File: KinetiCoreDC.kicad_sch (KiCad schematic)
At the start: 7 parts, among them J2 TC2070-IDC-NL, SW1 PTS647, U1 STM32G070KBT6

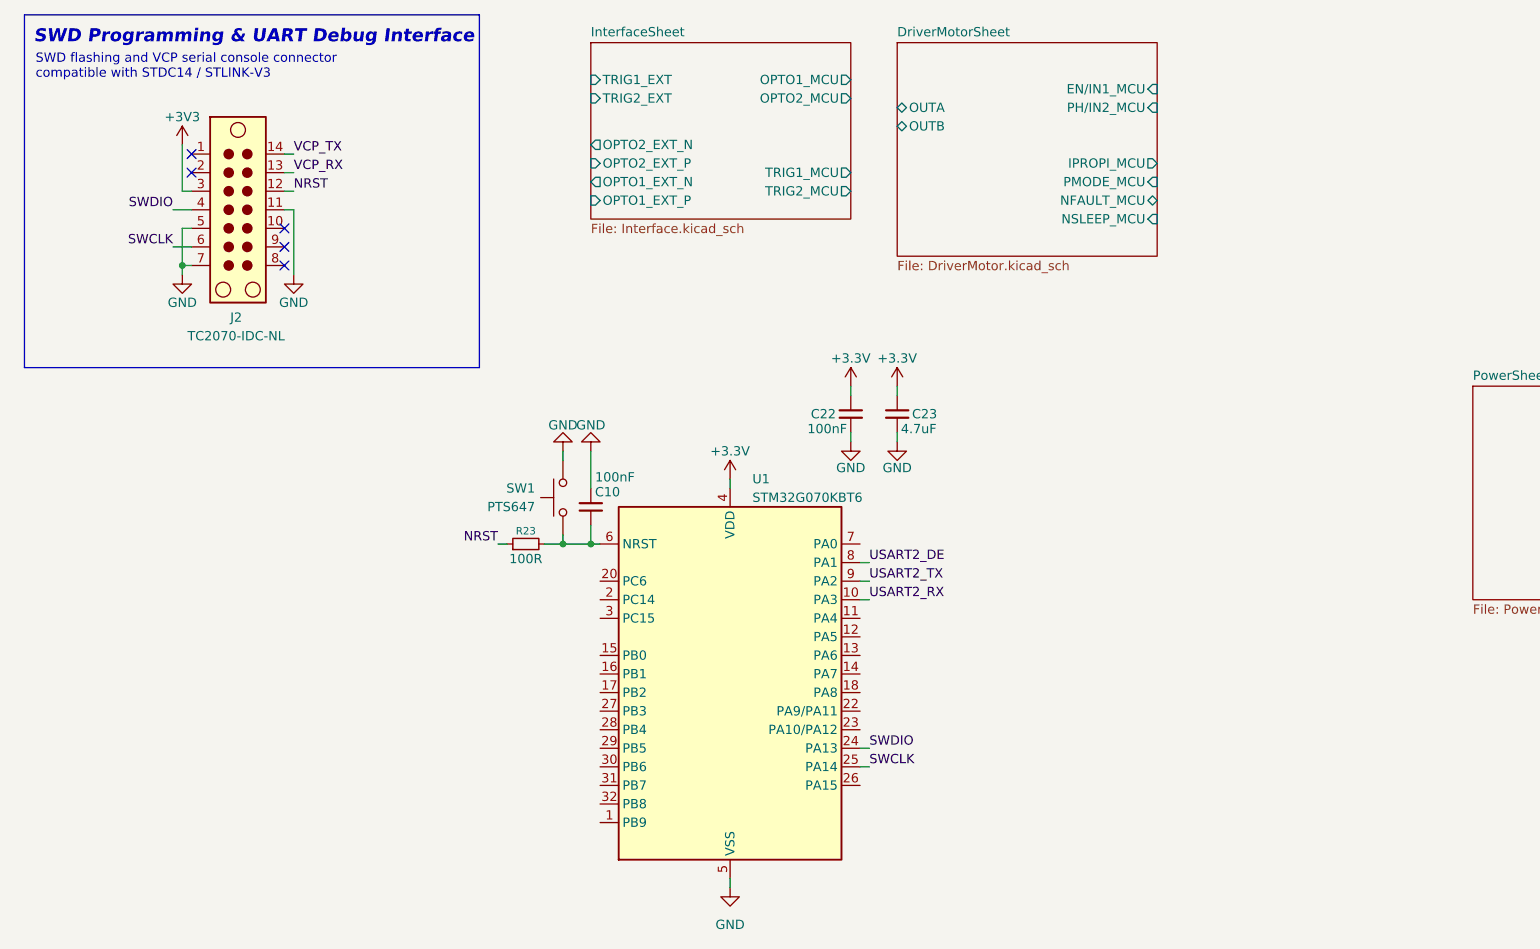
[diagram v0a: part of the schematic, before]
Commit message: feat: add LTC4365 protection circuit and 3.3V logic LDO
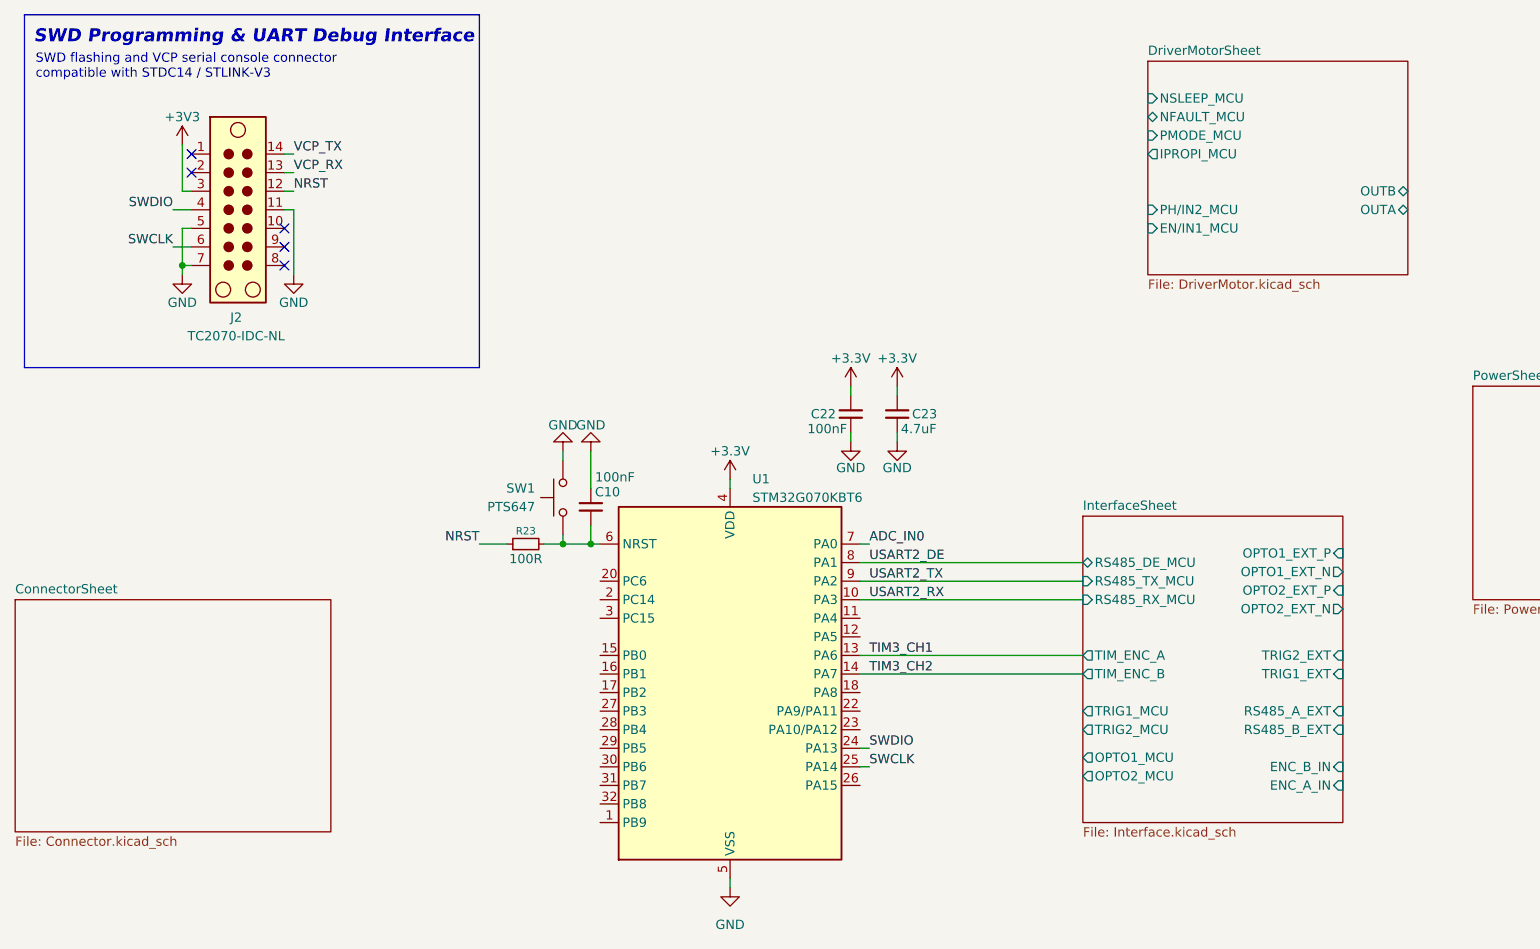
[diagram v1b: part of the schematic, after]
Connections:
- net TIM3_CH1: now reaches U1.13 (PA6)
- net TIM3_CH2: now reaches U1.14 (PA7)
- net ADC_IN0: now reaches U1.7 (PA0)
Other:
- added sheet ConnectorSheet (Connector.kicad_sch)
- sheet InterfaceSheet ports: added ENC_A_IN, ENC_B_IN, RS485_A_EXT, RS485_B_EXT, RS485_DE_MCU, RS485_RX_MCU, RS485_TX_MCU, TIM_ENC_A, TIM_ENC_B; removed none

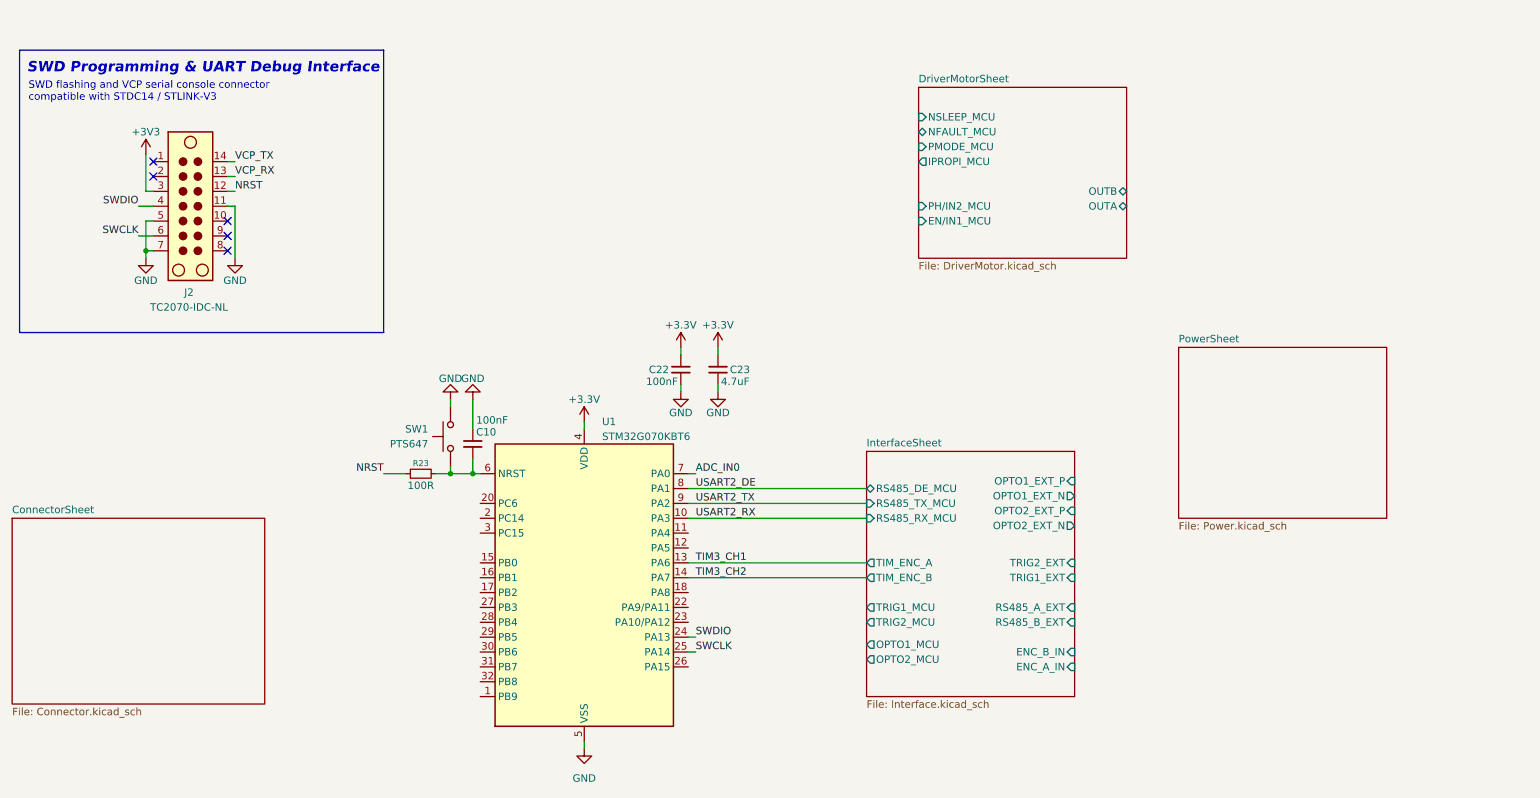
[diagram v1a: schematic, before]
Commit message: feat: add standardized functional notes across all schematic sheets
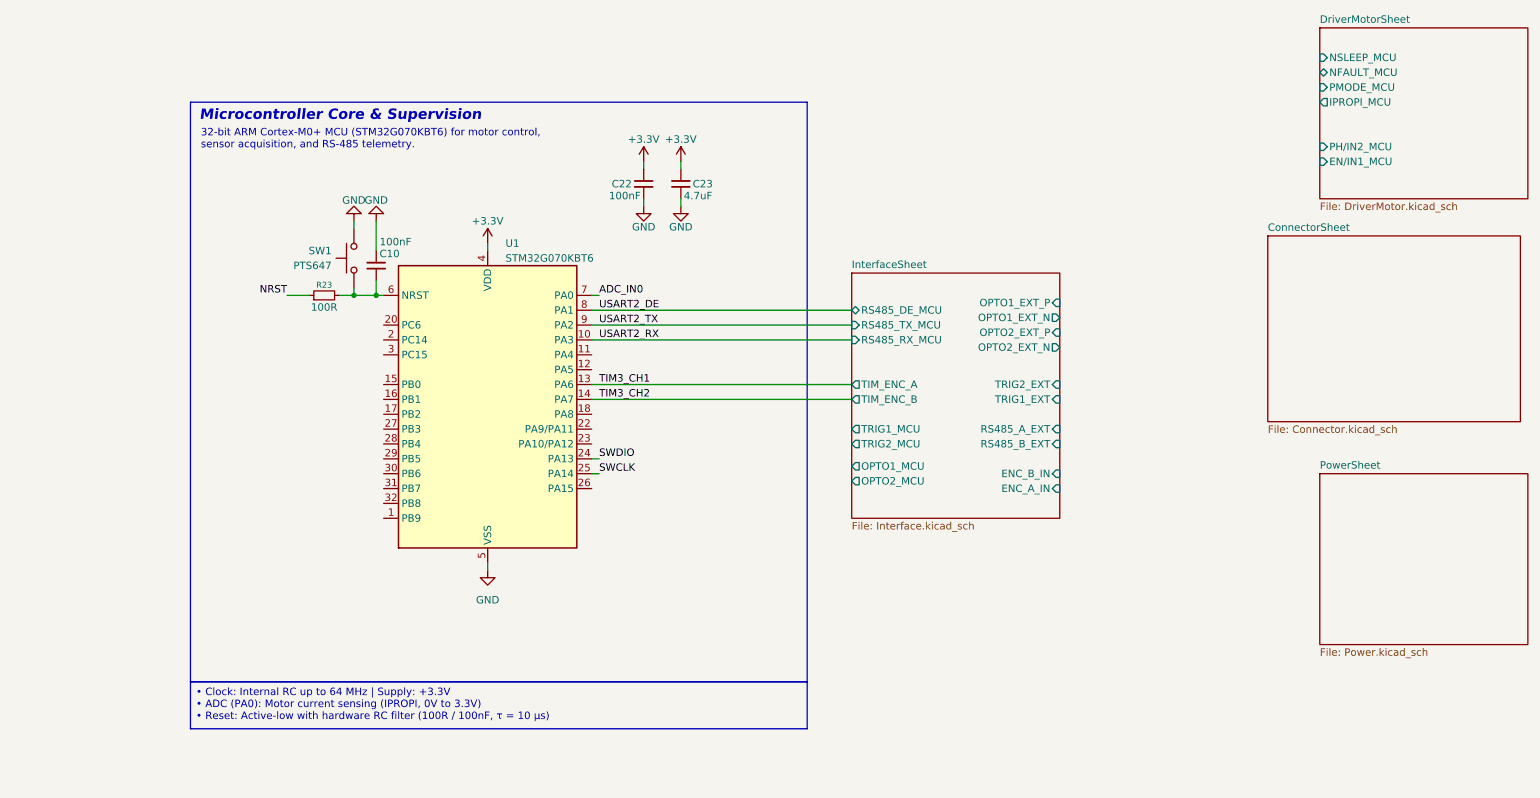
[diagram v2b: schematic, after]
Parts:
- removed J2: TC2070-IDC-NL, Library:Tag-Connect_TC2070-IDC-FP_2x07_P1.27mm_Vertical, symbol Connector:TC2070
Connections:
- no-connect marks 5 -> 0
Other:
- sheet DriverMotorSheet ports: added none; removed OUTA, OUTB
- note added: "32-bit ARM Cortex-M0+ MCU (STM32G070KBT6) for motor control, sensor acquisition, and RS-485 telemetry."
- note added: "Microcontroller Core & Supervision"
- note removed: "SWD Programming & UART Debug Interface"
- note removed: "SWD flashing and VCP serial console connector compatible with STDC14 / STLINK-V3"
- moved on the sheet: C10, C22, C23, R23, SW1, U1

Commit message: fix: fix some errors in shematic
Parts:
- renumbered C10 to C1, C22 to C2, C23 to C3, R23 to R1
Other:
- moved on the sheet: C1, C2, C3, R1, SW1, U1

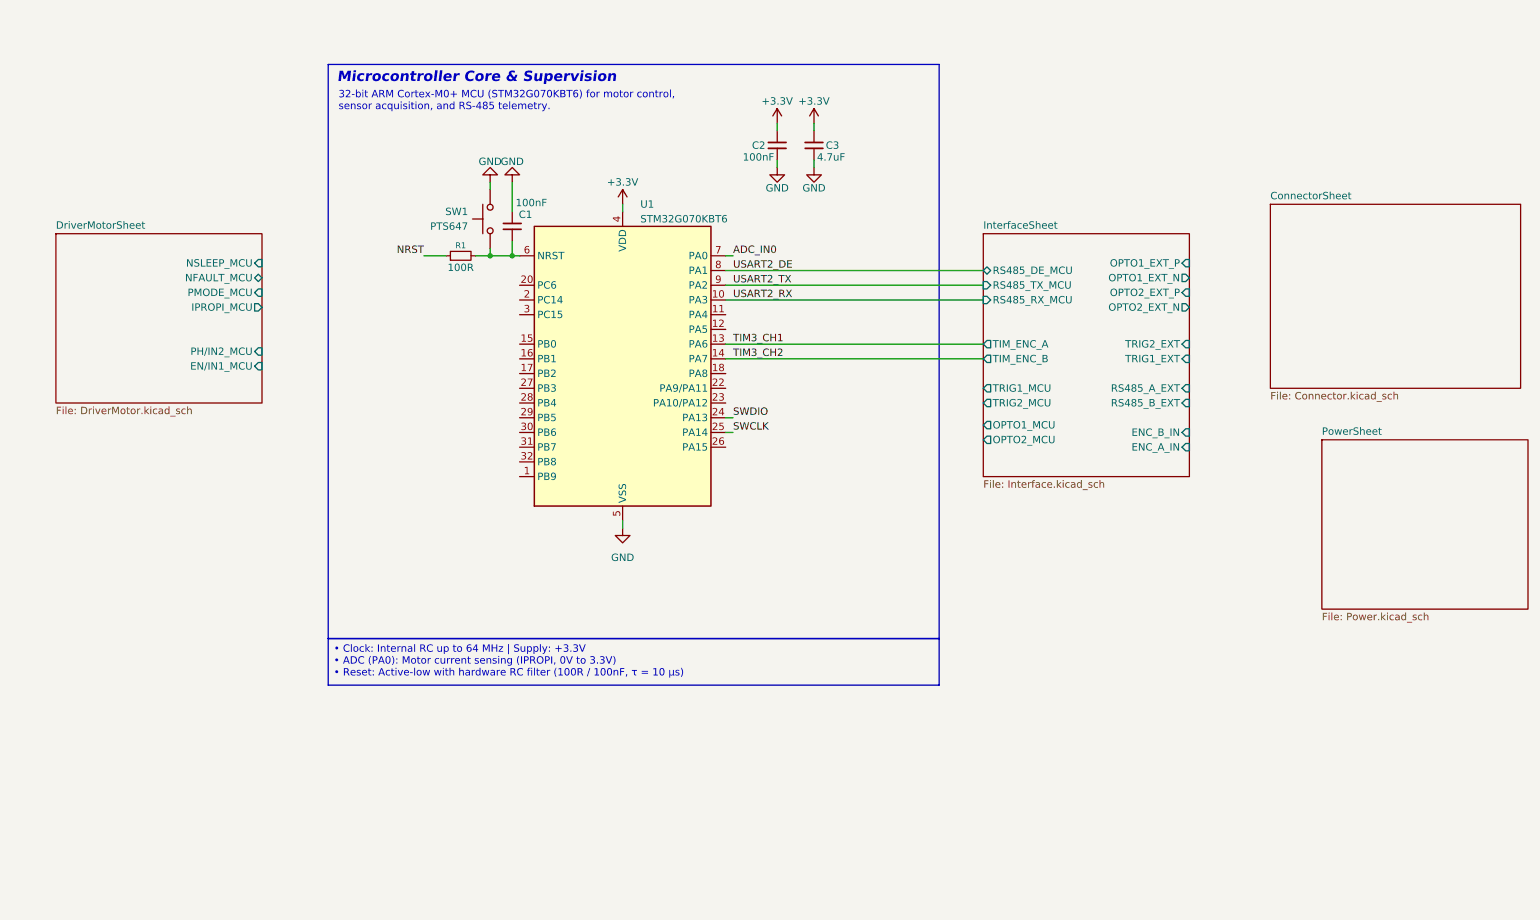
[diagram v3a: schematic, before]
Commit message: wip(sch): draft JST-XH and solder pad connector interfaces
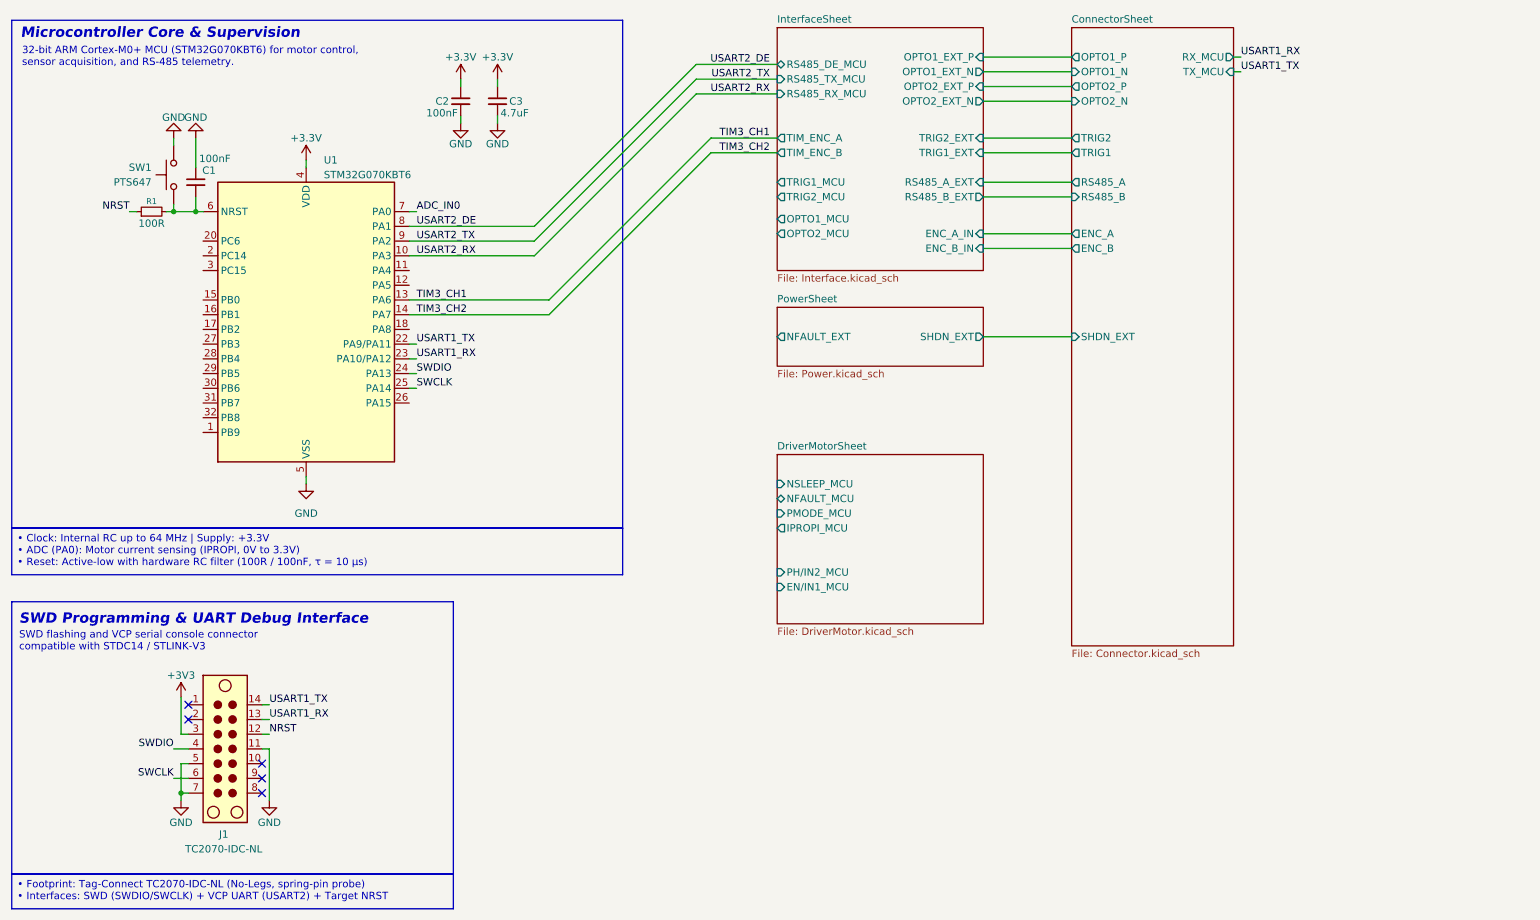
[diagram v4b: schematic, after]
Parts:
- added J1: TC2070-IDC-NL, KineticCore:Tag-Connect_TC2070-IDC-FP_2x07_P1.27mm_Vertical, symbol Connector:TC2070
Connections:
- net GND: now also J1.11, J1.5, J1.7
- net NRST: now also J1.12
- net SWCLK: now also J1.6
- net SWDIO: now also J1.4
- net USART1_TX: now reaches U1.22 (PA9/PA11)
- net USART1_TX: now also J1.14
- net USART1_RX: now reaches U1.23 (PA10/PA12)
- net USART1_RX: now also J1.13
- new net +3V3: J1.3
- no-connect marks 0 -> 5
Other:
- sheet ConnectorSheet ports: added ENC_A, ENC_B, OPTO1_N, OPTO1_P, OPTO2_N, OPTO2_P, RS485_A, RS485_B, RX_MCU, SHDN_EXT, TRIG1, TRIG2, TX_MCU; removed none
- sheet PowerSheet ports: added NFAULT_EXT, SHDN_EXT; removed none
- note added: "SWD Programming & UART Debug Interface"
- note added: "SWD flashing and VCP serial console connector compatible with STDC14 / STLINK-V3"
- moved on the sheet: C1, C2, C3, R1, SW1, U1
